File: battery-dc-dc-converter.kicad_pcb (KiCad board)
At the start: 2 copper layers, 42 x 33 mm, 22 parts, among them J1 Conn_01x02, J2 Conn_01x01, J3 Conn_01x01, U1 LMR16020

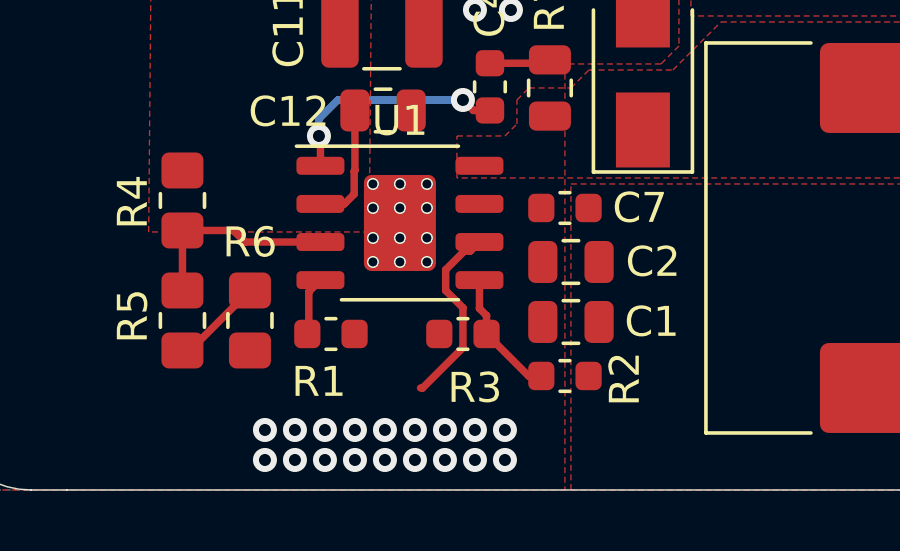
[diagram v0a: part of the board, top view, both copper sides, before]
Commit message: Added dc-dc v0.2 text
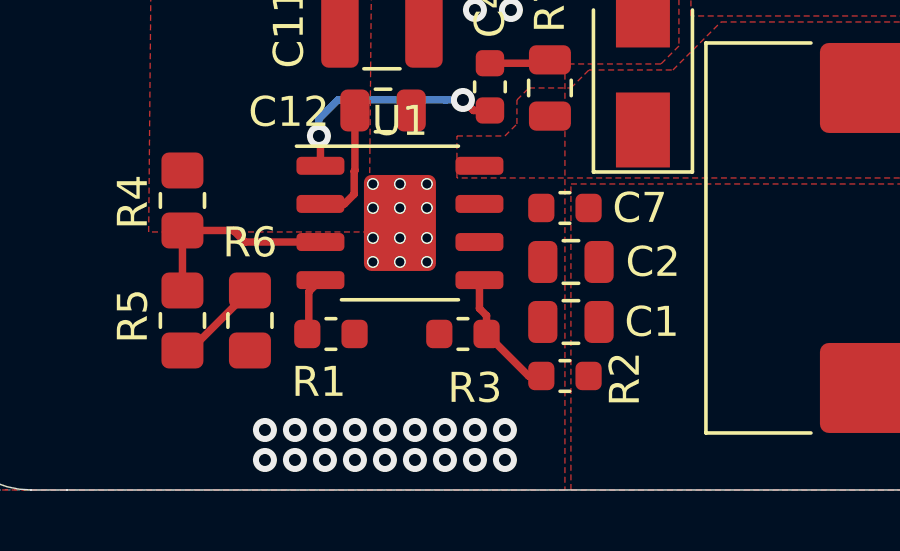
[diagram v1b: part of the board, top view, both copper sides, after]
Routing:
- net Net-(U1-Pad6): track 6.31 -> 0.00 mm
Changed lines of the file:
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@@
     (thickness 1.6)
     (drawings 41)
-    (tracks 106)
+    (tracks 98)
     (zones 0)
     (modules 22)
@@
   (page A4)
   (layers
-    (0 F.Cu signal)
-    (31 B.Cu signal)
+    (0 F.Cu signal hide)
+    (31 B.Cu signal hide)
     (32 B.Adhes user)
     (33 F.Adhes user)
@@
   (gr_line (start 81.4 25.5) (end 81.4 44.5) (layer B.SilkS) (width 0.12))
   (gr_line (start 63.4 25.5) (end 81.4 25.5) (layer B.SilkS) (width 0.12))
-  (gr_text Vin (at 114 37) (layer B.SilkS)
+  (gr_text Vin (at 113 36.4) (layer B.SilkS)
     (effects (font (size 1 1) (thickness 0.15)) (justify mirror))
   )
-  (gr_text Gnd (at 107 37) (layer B.SilkS)
+  (gr_text Gnd (at 106.5 36.6) (layer B.SilkS)
     (effects (font (size 1 1) (thickness 0.15)) (justify mirror))
   )
@@
   (segment (start 106.5 63.55) (end 108.5 61.55) (width 0.25) (layer F.Cu) (net 8) (status 30))
   (segment (start 106.25 63.55) (end 106.5 63.55) (width 0.25) (layer F.Cu) (net 8) (status 30))
-  (segment (start 114.256494 64.8) (end 115.6 63.456494) (width 0.25) (layer F.Cu) (net 13))
-  (segment (start 114.1875 64.8) (end 114.256494 64.8) (width 0.25) (layer F.Cu) (net 13))
-  (segment (start 115.648232 60.235) (end 115.85 60.235) (width 0.25) (layer F.Cu) (net 13))
-  (segment (start 115.02499 61.551758) (end 115.02499 60.858242) (width 0.25) (layer F.Cu) (net 13))
-  (segment (start 115.85 60.235) (end 116.15 59.935) (width 0.25) (layer F.Cu) (net 13) (status 20))
-  (segment (start 115.02499 60.858242) (end 115.648232 60.235) (width 0.25) (layer F.Cu) (net 13))
-  (segment (start 115.6 62.126768) (end 115.02499 61.551758) (width 0.25) (layer F.Cu) (net 13))
-  (segment (start 115.6 63.456494) (end 115.6 62.126768) (width 0.25) (layer F.Cu) (net 13))
   (via (at 115.6 55.2) (size 0.8) (drill 0.4) (layers F.Cu B.Cu) (net 10))
   (segment (start 115.95 55.55) (end 115.6 55.2) (width 0.25) (layer F.Cu) (net 10))

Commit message: Order v0.2
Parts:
- added C3: 220nF, Capacitor_SMD:C_0805_2012Metric, F.Cu at (112.9, 53.5)
- C7: renamed from C12; value 470nF -> 220nF
- moved C5 2.15 mm to (112.8, 47.4)
- moved C6 2.00 mm to (112.9, 50.8)
- moved F1 1.43 mm to (109.2, 45.1)
- moved J1 0.60 mm to (109.6, 40.6)
- renumbered C10 to C5, C11 to C6, C7 to C8
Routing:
- net GND: vias 47 -> 41
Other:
- board text added: "DC-DC V0.2"
- board text removed: "20-42V to 12V 3A DC-DC Converter"
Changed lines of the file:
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@@
   (general
     (thickness 1.6)
-    (drawings 41)
-    (tracks 98)
+    (drawings 38)
+    (tracks 92)
     (zones 0)
-    (modules 22)
+    (modules 23)
     (nets 14)
   )
   (page A4)
   (layers
-    (0 F.Cu signal hide)
-    (31 B.Cu signal hide)
+    (0 F.Cu signal)
+    (31 B.Cu signal)
     (32 B.Adhes user)
     (33 F.Adhes user)
@@
       (drillshape 0)
       (scaleselection 1)
-      (outputdirectory "fabrication-output/v3/"))
+      (outputdirectory "fabrication-output/dc-dc-v0.2/"))
   )
   (net 0 "")
@@
   (module battery-dc-dc-converter:SWRH1207B (layer F.Cu)
     (at 130.2 59.8 270)
+    (attr smd)
     (fp_text reference L1 (at 0 -7.5 90) (layer F.SilkS)
       (effects (font (size 1 1) (thickness 0.15)))
@@
     (tags capacitor)
     (attr smd)
-    (fp_text reference C7 (at -2.5 0 180) (layer F.SilkS)
+    (fp_text reference C8 (at -2.5 0 180) (layer F.SilkS)
       (effects (font (size 1 1) (thickness 0.15)))
     )
@@
   )
   (module Capacitor_SMD:C_0805_2012Metric (layer F.Cu)
-    (at 112.9375 55.55)
+    (at 112.9 55.55)
     (descr "Capacitor SMD 0805 (2012 Metric), square (rectangular) end terminal, IPC_7351 nominal, (Body size source: https://docs.google.com/spreadsheets/d/1BsfQQcO9C6DZCsRaXUlFlo91Tg2WpOkGARC1WS5S8t0/edit?usp=sharing), generated with kicad-footprint-generator")
     (tags capacitor)
     (attr smd)
-    (fp_text reference C12 (at -3.1375 0.05) (layer F.SilkS)
-      (effects (font (size 1 1) (thickness 0.15)))
-    )
-    (fp_text value 470nF (at 0 1.65) (layer F.Fab)
+    (fp_text reference C7 (at -3.1375 0.05) (layer F.SilkS)
+      (effects (font (size 1 1) (thickness 0.15)))
+    )
+    (fp_text value 220nF (at 0 1.65) (layer F.Fab)
       (effects (font (size 1 1) (thickness 0.15)))
     )
@@
   )
   (module scooter-ps:xt60pw-m (layer B.Cu)
-    (at 110.2 40.6)
+    (at 109.6 40.6)
     (fp_text reference J1 (at 0.4 -5.1) (layer B.SilkS) hide
       (effects (font (size 1 1) (thickness 0.15)) (justify mirror))
@@
   )
   (module Fuse:Fuse_1206_3216Metric_Pad1.42x1.75mm_HandSolder (layer F.Cu)
-    (at 110.6 44.8 90)
+    (at 109.2 45.1 90)
     (descr "Fuse SMD 1206 (3216 Metric), square (rectangular) end terminal, IPC_7351 nominal with elongated pad for handsoldering. (Body size source: http://www.tortai-tech.com/upload/download/2011102023233369053.pdf), generated with kicad-footprint-generator")
     (tags "fuse handsolder")
     (attr smd)
-    (fp_text reference F1 (at 0.1875 1.9 90) (layer F.SilkS)
+    (fp_text reference F1 (at 0.1 -1.9 90) (layer F.SilkS)
       (effects (font (size 1 1) (thickness 0.15)))
     )
@@
   )
   (module Capacitor_SMD:C_1210_3225Metric (layer F.Cu)
-    (at 112.9 49.55)
+    (at 112.8 47.4)
     (descr "Capacitor SMD 1210 (3225 Metric), square (rectangular) end terminal, IPC_7351 nominal, (Body size source: http://www.tortai-tech.com/upload/download/2011102023233369053.pdf), generated with kicad-footprint-generator")
     (tags capacitor)
     (attr smd)
-    (fp_text reference C10 (at -3.1 0.05 270) (layer F.SilkS)
+    (fp_text reference C5 (at -3.8 1.3) (layer F.SilkS)
       (effects (font (size 1 1) (thickness 0.15)))
     )
@@
   )
   (module Capacitor_SMD:C_1210_3225Metric (layer F.Cu)
-    (at 112.9 52.8)
+    (at 112.9 50.8)
     (descr "Capacitor SMD 1210 (3225 Metric), square (rectangular) end terminal, IPC_7351 nominal, (Body size source: http://www.tortai-tech.com/upload/download/2011102023233369053.pdf), generated with kicad-footprint-generator")
     (tags capacitor)
     (attr smd)
-    (fp_text reference C11 (at -3.1 0 270) (layer F.SilkS)
+    (fp_text reference C6 (at -3.7 0.7) (layer F.SilkS)
       (effects (font (size 1 1) (thickness 0.15)))
     )
@@
     (tags "HTSOP SO")
     (attr smd)
-    (fp_text reference U1 (at 0 -3.4) (layer F.SilkS)
+    (fp_text reference U1 (at -4.6 -2.1) (layer F.SilkS)
       (effects (font (size 1 1) (thickness 0.15)))
     )
@@
     )
   )
+  (module Capacitor_SMD:C_0805_2012Metric (layer F.Cu)
+    (at 112.9 53.5)
+    (descr "Capacitor SMD 0805 (2012 Metric), square (rectangular) end terminal, IPC_7351 nominal, (Body size source: https://docs.google.com/spreadsheets/d/1BsfQQcO9C6DZCsRaXUlFlo91Tg2WpOkGARC1WS5S8t0/edit?usp=sharing), generated with kicad-footprint-generator")
+    (tags capacitor)
+    (attr smd)
+    (fp_text reference C3 (at -2.8 0.1) (layer F.SilkS)
+      (effects (font (size 1 1) (thickness 0.15)))
+    )
+    (fp_text value 220nF (at 0 1.65) (layer F.Fab)
+      (effects (font (size 1 1) (thickness 0.15)))
+    )
+    (fp_line (start -1 0.6) (end -1 -0.6) (layer F.Fab) (width 0.1))
+    (fp_line (start -1 -0.6) (end 1 -0.6) (layer F.Fab) (width 0.1))
+    (fp_line (start 1 -0.6) (end 1 0.6) (layer F.Fab) (width 0.1))
+    (fp_line (start 1 0.6) (end -1 0.6) (layer F.Fab) (width 0.1))
+    (fp_line (start -0.258578 -0.71) (end 0.258578 -0.71) (layer F.SilkS) (width 0.12))
+    (fp_line (start -0.258578 0.71) (end 0.258578 0.71) (layer F.SilkS) (width 0.12))
+    (fp_line (start -1.68 0.95) (end -1.68 -0.95) (layer F.CrtYd) (width 0.05))
+    (fp_line (start -1.68 -0.95) (end 1.68 -0.95) (layer F.CrtYd) (width 0.05))
+    (fp_line (start 1.68 -0.95) (end 1.68 0.95) (layer F.CrtYd) (width 0.05))
+    (fp_line (start 1.68 0.95) (end -1.68 0.95) (layer F.CrtYd) (width 0.05))
+    (fp_text user %R (at 0 0) (layer F.Fab)
+      (effects (font (size 0.5 0.5) (thickness 0.08)))
+    )
+    (pad 1 smd roundrect (at -0.9375 0) (size 0.975 1.4) (layers F.Cu F.Paste F.Mask) (roundrect_rratio 0.25)
+      (net 3 VCC))
+    (pad 2 smd roundrect (at 0.9375 0) (size 0.975 1.4) (layers F.Cu F.Paste F.Mask) (roundrect_rratio 0.25)
+      (net 1 GND))
+    (model ${KISYS3DMOD}/Capacitor_SMD.3dshapes/C_0805_2012Metric.wrl
+      (at (xyz 0 0 0))
+      (scale (xyz 1 1 1))
+      (rotate (xyz 0 0 0))
+    )
+  )
+  (gr_text "DC-DC V0.2" (at 118.8 63.1) (layer B.SilkS)
+    (effects (font (size 2 2) (thickness 0.2)) (justify mirror))
+  )
   (dimension 42 (width 0.15) (layer F.Fab)
     (gr_text "42.000 mm" (at 119.2 26.150001) (layer F.Fab)
@@
   (gr_line (start 140.2 38.8) (end 140.2 38.2) (layer Edge.Cuts) (width 0.05))
   (gr_line (start 140.2 64.4) (end 140.2 65.2) (layer Edge.Cuts) (width 0.05))
-  (gr_line (start 63.4 44.5) (end 63.4 25.5) (layer B.SilkS) (width 0.12))
-  (gr_line (start 81.4 25.5) (end 81.4 44.5) (layer B.SilkS) (width 0.12))
-  (gr_line (start 63.4 25.5) (end 81.4 25.5) (layer B.SilkS) (width 0.12))
   (gr_text Vin (at 113 36.4) (layer B.SilkS)
     (effects (font (size 1 1) (thickness 0.15)) (justify mirror))
@@
   (gr_text Gnd (at 106.5 36.6) (layer B.SilkS)
     (effects (font (size 1 1) (thickness 0.15)) (justify mirror))
-  )
-  (gr_text "20-42V to 12V 3A \nDC-DC Converter" (at 66.2 90.95) (layer B.SilkS)
-    (effects (font (size 2 2) (thickness 0.3)) (justify mirror))
   )
   (gr_text Gnd (at 132.2 36.2 180) (layer F.SilkS)
@@
   (segment (start 116.15 58.665) (end 115.615 58.665) (width 0.25) (layer F.Cu) (net 1) (status 30))
   (segment (start 111.7375 63) (end 111.9875 63) (width 0.25) (layer F.Cu) (net 1) (status 30))
-  (via (at 113.6 45.2) (size 0.8) (drill 0.4) (layers F.Cu B.Cu) (net 1))
-  (via (at 114.8 45.2) (size 0.8) (drill 0.4) (layers F.Cu B.Cu) (net 1))
   (via (at 116 45.2) (size 0.8) (drill 0.4) (layers F.Cu B.Cu) (net 1))
-  (via (at 113.6 46.2) (size 0.8) (drill 0.4) (layers F.Cu B.Cu) (net 1))
-  (via (at 114.8 46.2) (size 0.8) (drill 0.4) (layers F.Cu B.Cu) (net 1))
-  (via (at 113.6 47.2) (size 0.8) (drill 0.4) (layers F.Cu B.Cu) (net 1))
-  (via (at 114.8 47.2) (size 0.8) (drill 0.4) (layers F.Cu B.Cu) (net 1))
   (via (at 116 49.2) (size 0.8) (drill 0.4) (layers F.Cu B.Cu) (net 1))
   (via (at 117.2 49.2) (size 0.8) (drill 0.4) (layers F.Cu B.Cu) (net 1))
@@
     (polygon
       (pts
-        (xy 118.2 44) (xy 109.6 44) (xy 109.6 35.8) (xy 118.2 35.8)
+        (xy 118.2 44.4) (xy 108.3 44.4) (xy 108.3 35.8) (xy 118.2 35.8)
       )
     )

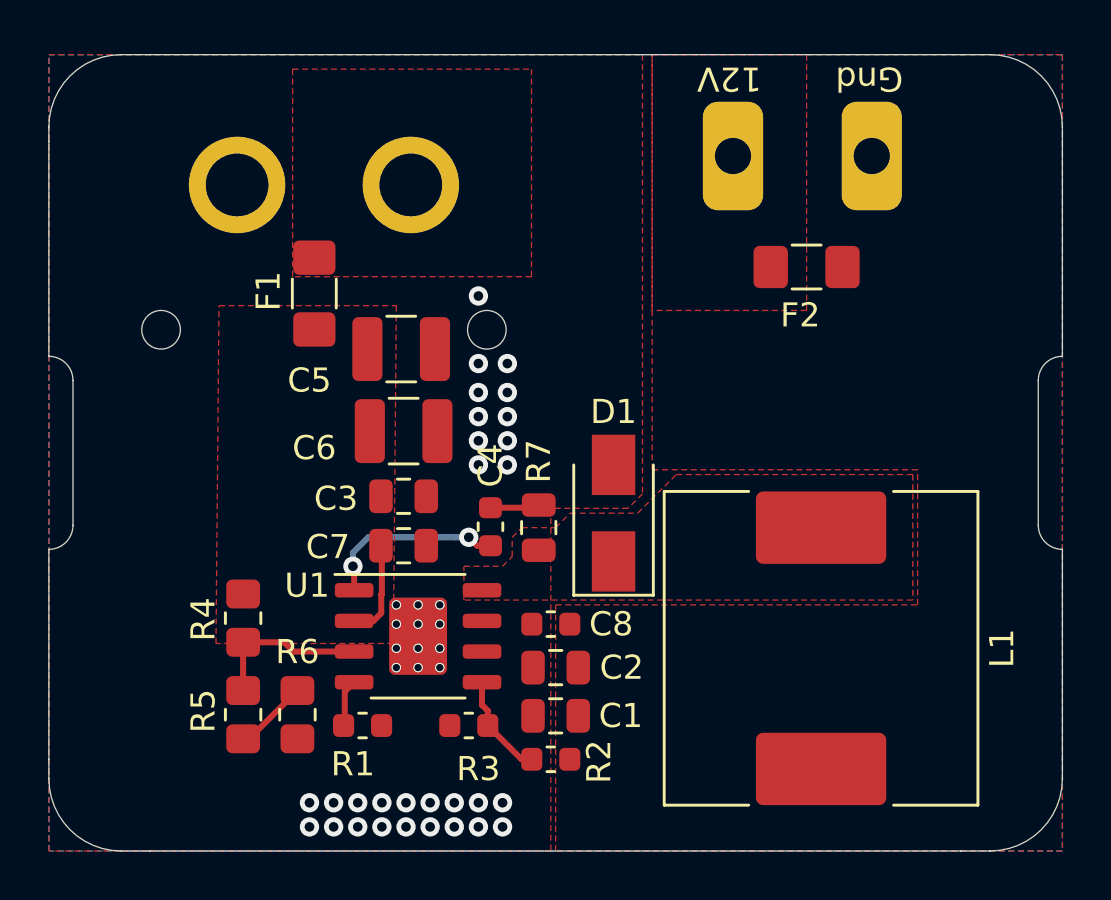
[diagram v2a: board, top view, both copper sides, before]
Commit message: Put power plug on same side
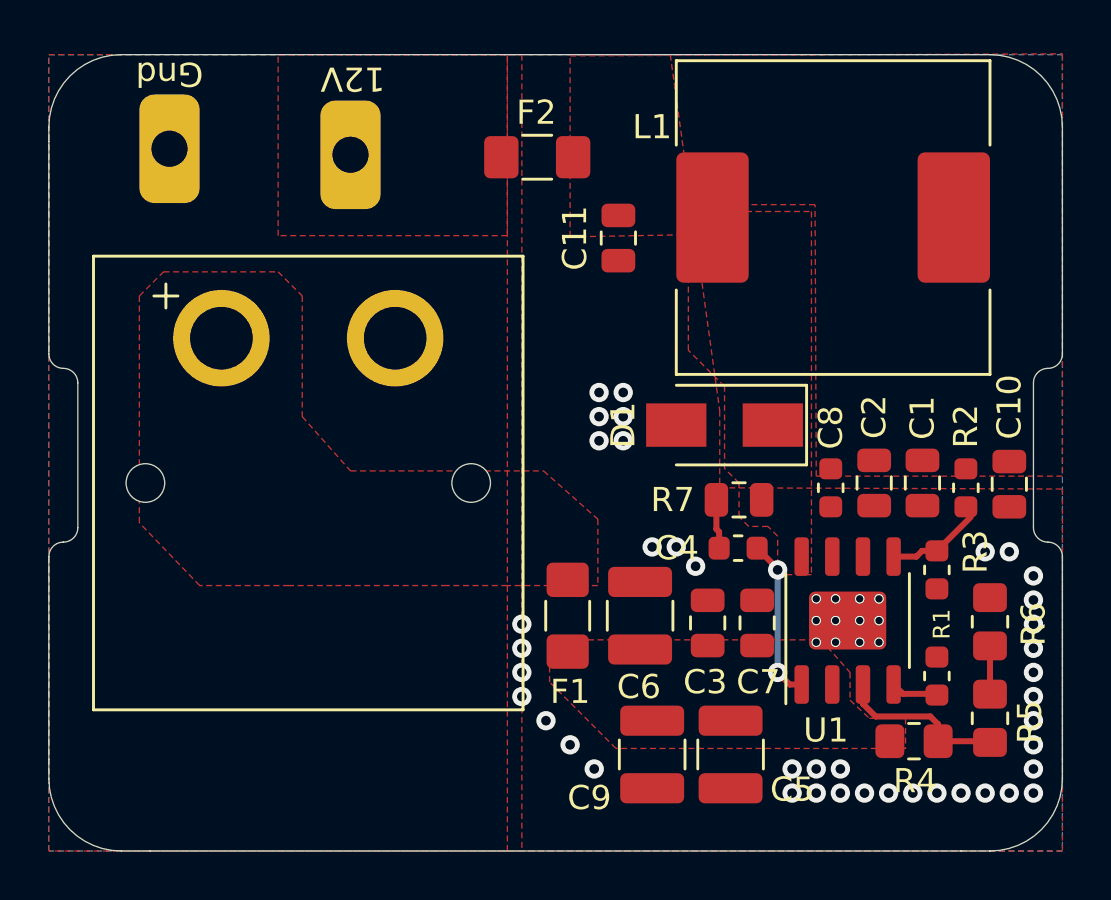
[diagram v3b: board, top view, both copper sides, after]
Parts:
- added C10: 22uF, Capacitor_SMD:C_0805_2012Metric, F.Cu at (138.0, 53.0)
- added C11: 22uF, Capacitor_SMD:C_0805_2012Metric, F.Cu at (121.8, 42.8)
- added C9: 2.2uF, Capacitor_SMD:C_1210_3225Metric, F.Cu at (123.2, 64.2)
- J1: moved to F.Cu
- R7: value 3R3 -> 3.3R
- moved R5 31.0 mm to (137.2, 62.7), turned to 90 degrees
- moved J3 29.1 mm to (103.2, 39.2)
- moved R6 29.0 mm to (137.2, 58.7), turned to 90 degrees
- moved R4 28.3 mm to (134.1, 63.6), turned to 0 degrees
- moved R1 23.9 mm to (135.0, 61.0), turned to 90 degrees
- moved C5 21.6 mm to (126.5, 64.2), turned to 270 degrees
- moved R2 20.6 mm to (136.2, 53.1), turned to 270 degrees
- moved R3 20.4 mm to (135.0, 56.5), turned to 270 degrees
- moved C1 18.0 mm to (134.4, 53.0), turned to 270 degrees
- moved L1 17.9 mm to (130.7, 42.0), turned to 0 degrees
- moved U1 17.8 mm to (131.3, 58.6), turned to 90 degrees
- moved F1 17.0 mm to (119.7, 58.5)
- moved J2 15.9 mm to (110.7, 39.5)
- moved C2 15.3 mm to (132.4, 53.0), turned to 270 degrees
- moved C7 15.0 mm to (127.5, 58.8), turned to 90 degrees
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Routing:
- net VCC: track 4.06 -> 0.00 mm
- net Net-(C4-Pad2): track 7.97 -> 6.70 mm
- net Net-(R5-Pad2): track 3.08 -> 2.00 mm
- net GND: vias 41 -> 53
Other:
- outline, holes or cut-outs redrawn
- board text added: "DC-DC V0.3.0"
- board text removed: "DC-DC V0.2"
- board text removed: "Vin"

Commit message: panelize WIP
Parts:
- removed C8: 1uF, Capacitor_SMD:C_0603_1608Metric
- removed R7: 3.3R, Resistor_SMD:R_0805_2012Metric
- added REF**: Tab, PCM_kikit:Tab, F.Cu at (131.4, 69.7)
- added REF**: Tab, PCM_kikit:Tab, F.Cu at (107.0, 69.6)
- added REF**: Tab, PCM_kikit:Tab, F.Cu at (107.0, 34.4)
- added REF**: Tab, PCM_kikit:Tab, F.Cu at (131.4, 34.2)
- added REF**: Tab, PCM_kikit:Tab, F.Cu at (140.4, 51.8)
- added REF**: Tab, PCM_kikit:Tab, F.Cu at (98.9, 51.8)
- R4, R5, R6: footprint Resistor_SMD:R_0805_2012Metric_Pad1.20x1.40mm_HandSolder -> Resistor_SMD:R_0603_1608Metric
- U1: value LMR16020 -> LMR16030P; footprint Package_SO:HTSOP-8-1EP_3.9x4.9mm_P1.27mm_EP2.4x3.2mm -> Package_SO:TI_SO-PowerPAD-8
- moved C2 20.9 mm to (119.0, 37.0), turned to 180 degrees
- moved C6 7.46 mm to (127.0, 64.5), turned to -90 degrees
- moved C5 5.43 mm to (123.1, 59.9), turned to 90 degrees
- moved D1 4.82 mm to (126.8, 55.3), turned to -90 degrees
- moved L1 3.50 mm to (128.4, 44.5), turned to 90 degrees
- moved C11 2.96 mm to (119.0, 41.9), turned to 180 degrees
- moved R6 2.68 mm to (136.2, 61.2)
- moved C4 2.56 mm to (124.4, 54.8), turned to -90 degrees
- moved R5 2.37 mm to (134.9, 63.4), turned to 0 degrees
- moved R4 2.10 mm to (132.0, 63.4)
- moved C3 1.80 mm to (125.7, 60.5)
- moved C7 1.79 mm to (127.6, 60.5)
- moved C1 1.60 mm to (132.8, 52.9)
- moved C10 1.52 mm to (136.5, 53.4)
- moved R2 1.49 mm to (134.7, 53.4)
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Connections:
- net Net-(C4-Pad2) renamed /Boot
- net Net-(R2-Pad2) renamed /FB
- net Net-(R4-Pad2) renamed /EN
- C4 pad 1: Net-(C4-Pad1) -> /SW
- D1 pad 1: Net-(D1-Pad1) -> /SW
- L1 pad 1: Net-(D1-Pad1) -> /SW
- U1 pad 6: Net-(U1-Pad6) -> unconnected-(U1-PGOOD-Pad6)
- U1 pad 8: Net-(D1-Pad1) -> /SW
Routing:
- net /EN: track 6.97 -> 3.82 mm
- net /SW: track 0.00 -> 2.76 mm
- net Net-(C4-Pad1): track 2.21 -> 0.00 mm
- net GND: track 14.0 -> 12.7 mm, vias 53 -> 54
- net /FB: track 3.87 -> 2.93 mm
- net /Boot: track 6.70 -> 7.48 mm
- added copper zone on F.Cu, net /SW
- added copper zone on In1.Cu, net GND
- added copper zone on In2.Cu, net GND
- removed copper zone on F.Cu, net Net-(D1-Pad1)
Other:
- copper layers 2 -> 4
- net class Default removed
- rule pad_to_mask_clearance: 0.05 -> 0
- board text added: "${TAG}"
- board text added: "DC-DC converter Vin: 13-60V Vout: 12V Max Out: 3A"
- board text removed: "DC-DC V0.3.0"
